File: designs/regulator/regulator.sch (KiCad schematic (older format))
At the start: 34 parts

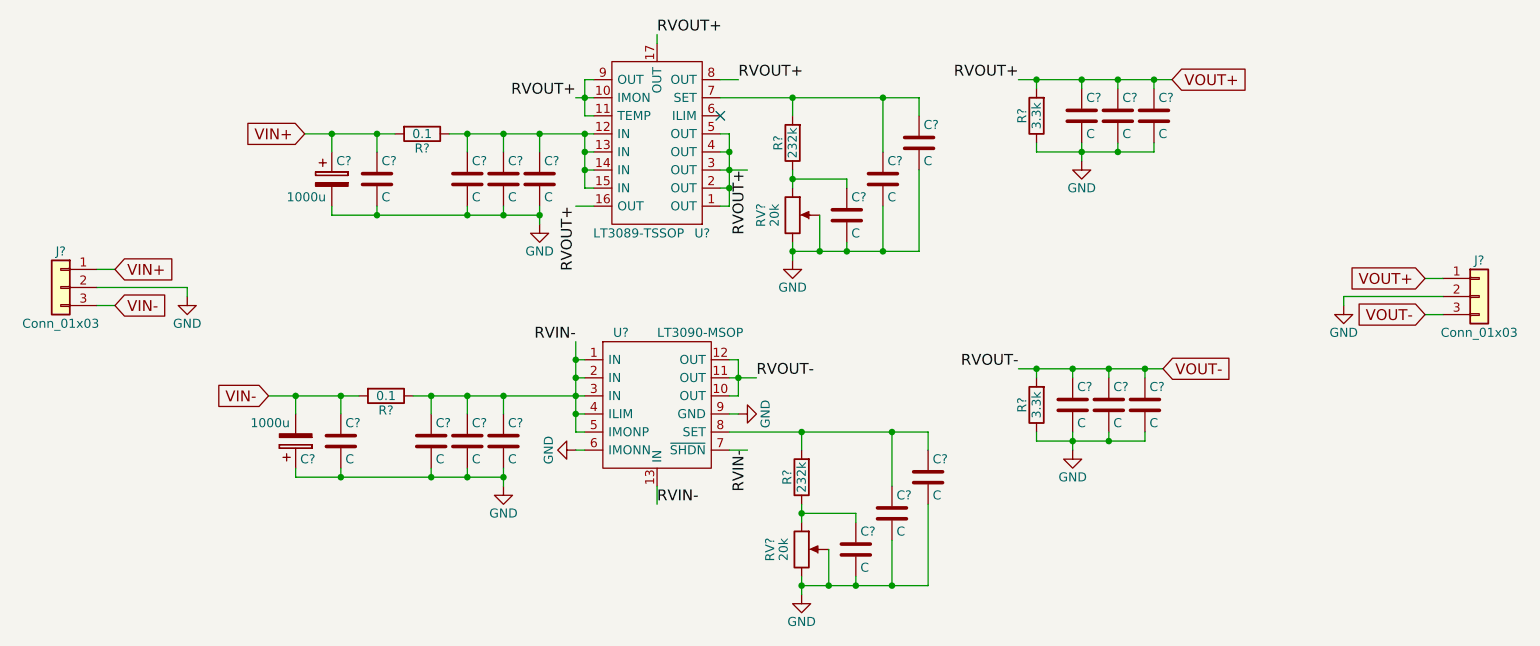
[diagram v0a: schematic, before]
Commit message: [designs/regulator] parts value and footprints
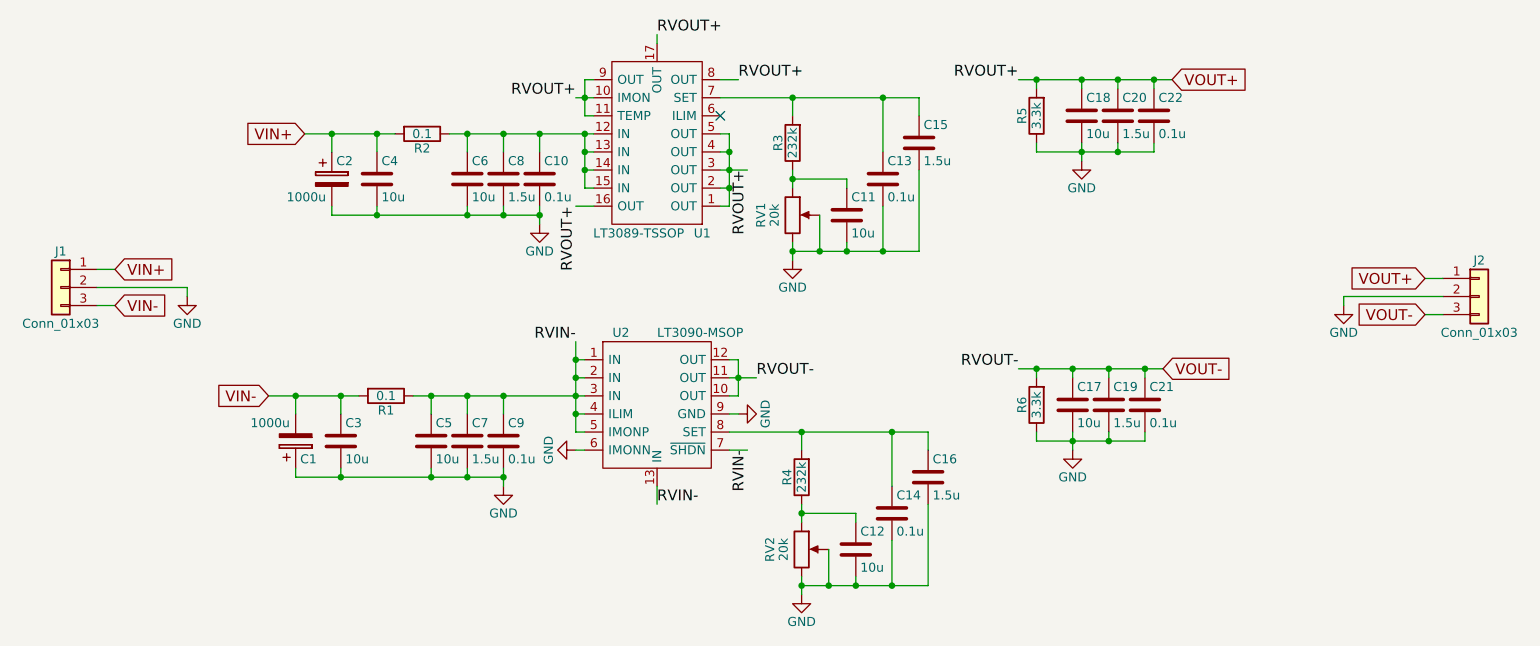
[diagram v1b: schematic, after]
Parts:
- C10, C13, C14, C21, C22, C9: renamed from C?; value C -> 0.1u; footprint (none) -> Capacitors_SMD:C_0805
- C11, C12, C17, C18, C3, C4, C5, C6: renamed from C?; value C -> 10u; footprint (none) -> Capacitors_SMD:C_0603
- C15, C16, C19, C20, C7, C8: renamed from C?; value C -> 1.5u; footprint (none) -> Capacitors_SMD:C_0805
- R1, R2, R3, R4, R5, R6: renamed from R?; footprint (none) -> Resistors_SMD:R_0603
- gave numbers to parts that had none: 8

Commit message: [designs/regulator] footprints of all parts
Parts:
- C1, C2: footprint (none) -> Capacitors2:CP_Elec_16x16
- J1, J2: footprint (none) -> Connectors2:3-pins_150mil
- RV1, RV2: footprint (none) -> Potentiometers:Potentiometer_Trimmer_Bourns_3269W
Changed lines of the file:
@@
 LIBS:valves
 LIBS:regulator
+LIBS:regulator-cache
 EELAYER 25 0
 EELAYER END
@@
 F 0 "J1" H 1950 4050 50  0000 C CNN
 F 1 "Conn_01x03" H 1950 3650 50  0000 C CNN
-F 2 "" H 1950 3850 50  0001 C CNN
+F 2 "Connectors2:3-pins_150mil" H 1950 3850 50  0001 C CNN
 F 3 "" H 1950 3850 50  0001 C CNN
 	1    1950 3850
@@
 F 0 "J2" H 9800 4100 50  0000 C CNN
 F 1 "Conn_01x03" H 9800 3700 50  0000 C CNN
-F 2 "" H 9800 3900 50  0001 C CNN
+F 2 "Connectors2:3-pins_150mil" H 9800 3900 50  0001 C CNN
 F 3 "" H 9800 3900 50  0001 C CNN
 	1    9800 3900
@@
 F 0 "C2" H 3475 3350 50  0000 L CNN
 F 1 "1000u" H 3200 3150 50  0000 L CNN
-F 2 "" H 3488 3100 50  0001 C CNN
+F 2 "Capacitors2:CP_Elec_16x16" H 3488 3100 50  0001 C CNN
 F 3 "" H 3450 3250 50  0001 C CNN
 	1    3450 3250
@@
 F 0 "RV1" V 5825 3450 50  0000 C CNN
 F 1 "20k" V 5900 3450 50  0000 C CNN
-F 2 "" H 6000 3450 50  0001 C CNN
+F 2 "Potentiometers:Potentiometer_Trimmer_Bourns_3269W" H 6000 3450 50  0001 C CNN
 F 3 "" H 6000 3450 50  0001 C CNN
 	1    6000 3450
@@
 F 0 "C1" H 3275 4800 50  0000 L CNN
 F 1 "1000u" H 3000 4600 50  0000 L CNN
-F 2 "" H 3288 4550 50  0001 C CNN
+F 2 "Capacitors2:CP_Elec_16x16" H 3288 4550 50  0001 C CNN
 F 3 "" H 3250 4700 50  0001 C CNN
 	1    3250 4700
@@
 F 0 "RV2" V 5875 5300 50  0000 C CNN
 F 1 "20k" V 5950 5300 50  0000 C CNN
-F 2 "" H 6050 5300 50  0001 C CNN
+F 2 "Potentiometers:Potentiometer_Trimmer_Bourns_3269W" H 6050 5300 50  0001 C CNN
 F 3 "" H 6050 5300 50  0001 C CNN
 	1    6050 5300

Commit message: [designs/regulator] Use throughwhole capacitor
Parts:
- C1, C2: value 1000u -> 100u; footprint Capacitors2:CP_Elec_16x16 -> Capacitors_THT:CP_Radial_D10.0mm_P5.00mm
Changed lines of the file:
@@
 P 3450 3250
 F 0 "C2" H 3475 3350 50  0000 L CNN
-F 1 "1000u" H 3200 3150 50  0000 L CNN
-F 2 "Capacitors2:CP_Elec_16x16" H 3488 3100 50  0001 C CNN
+F 1 "100u" H 3250 3150 50  0000 L CNN
+F 2 "Capacitors_THT:CP_Radial_D10.0mm_P5.00mm" H 3488 3100 50  0001 C CNN
 F 3 "" H 3450 3250 50  0001 C CNN
 	1    3450 3250
@@
 P 3250 4700
 F 0 "C1" H 3275 4800 50  0000 L CNN
-F 1 "1000u" H 3000 4600 50  0000 L CNN
-F 2 "Capacitors2:CP_Elec_16x16" H 3288 4550 50  0001 C CNN
+F 1 "100u" H 3050 4600 50  0000 L CNN
+F 2 "Capacitors_THT:CP_Radial_D10.0mm_P5.00mm" H 3288 4550 50  0001 C CNN
 F 3 "" H 3250 4700 50  0001 C CNN
 	1    3250 4700
@@
 	5650 4750 5750 4750
 Wire Wire Line
-	5250 4950 5250 5050
-Wire Wire Line
 	5700 4450 5650 4450
 Wire Wire Line
@@
 Wire Wire Line
 	7350 3100 8000 3100
+Wire Wire Line
+	5250 5050 5250 4950
 $EndSCHEMATC
